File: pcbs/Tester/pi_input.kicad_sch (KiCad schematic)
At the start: 9 parts, among them J201 Raspberry_Pi_2_3, J202 Conn_01x04, J203 Conn_01x10, U201 SN74LVC4245APWR, U202 SN74LVC4245APWR, U203 SN74LVC4245APWR

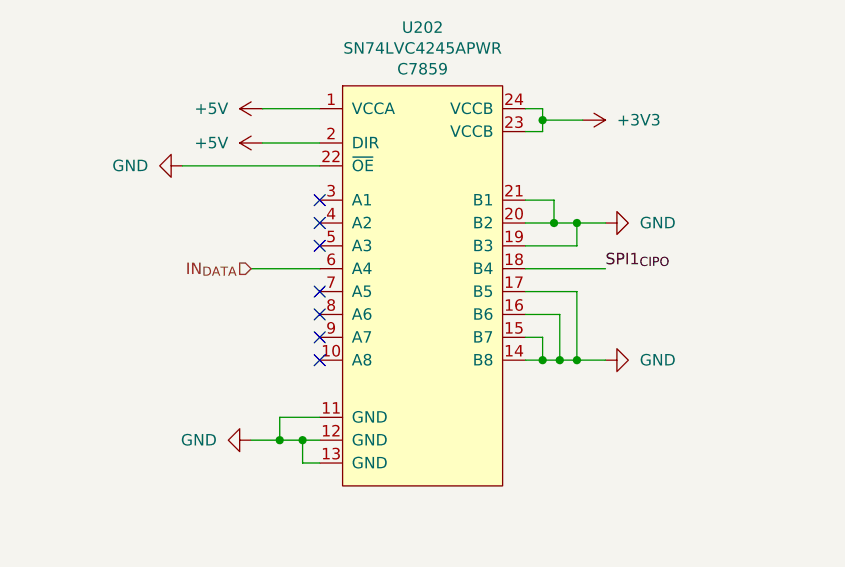
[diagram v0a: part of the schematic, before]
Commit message: Fix Tester board (#49)
The 'input' level shifter on the Tester board had the wrong set of pins connected to ground (copy paste error from the 'output' level shifters). This meant that the IC could effectively short circuit and become very hot. Switch over the ground and floating pins, to reflect how the inputs and outputs are for this IC.

Closes #47
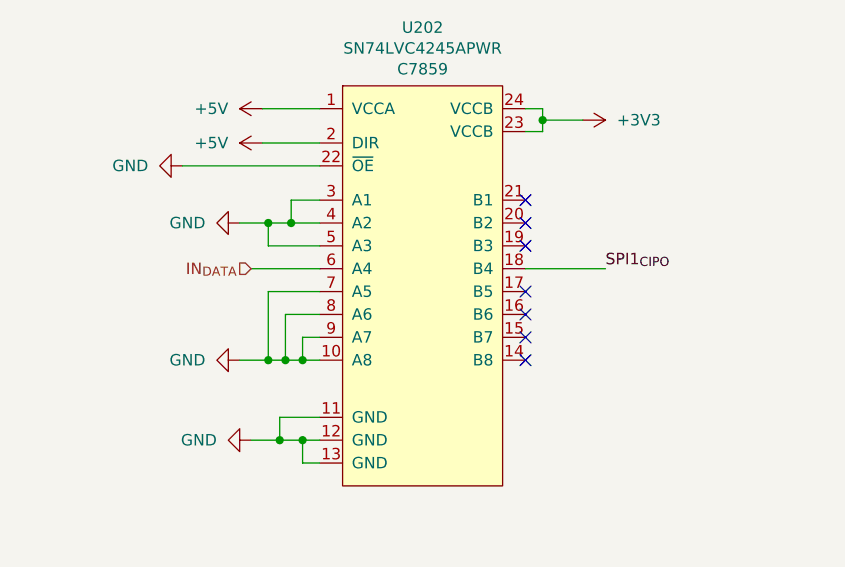
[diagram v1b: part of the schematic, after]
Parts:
- J203: footprint (none) -> Connector_PinHeader_2.54mm:PinHeader_1x10_P2.54mm_Vertical
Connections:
- net GND: now also U202.10 (A8), U202.3 (A1), U202.4 (A2), U202.5 (A3), U202.7 (A5), U202.8 (A6), U202.9 (A7); no longer U202.14 (B8), U202.15 (B7), U202.16 (B6), U202.17 (B5), U202.19 (B3), U202.20 (B2), U202.21 (B1)
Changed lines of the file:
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@@
   (junction (at 150.495 137.795) (diameter 0) (color 0 0 0 0)
   )
-  (junction (at 183.515 128.905) (diameter 0) (color 0 0 0 0)
+  (junction (at 149.225 128.905) (diameter 0) (color 0 0 0 0)
   )
   (junction (at 71.12 130.81) (diameter 0) (color 0 0 0 0)
@@
   (junction (at 74.93 130.81) (diameter 0) (color 0 0 0 0)
   )
-  (junction (at 183.515 113.665) (diameter 0) (color 0 0 0 0)
+  (junction (at 149.225 113.665) (diameter 0) (color 0 0 0 0)
   )
   (junction (at 76.2 130.81) (diameter 0) (color 0 0 0 0)
   )
-  (junction (at 180.975 113.665) (diameter 0) (color 0 0 0 0)
-  )
-  (junction (at 181.61 128.905) (diameter 0) (color 0 0 0 0)
-  )
-  (junction (at 179.705 128.905) (diameter 0) (color 0 0 0 0)
+  (junction (at 151.765 113.665) (diameter 0) (color 0 0 0 0)
+  )
+  (junction (at 151.13 128.905) (diameter 0) (color 0 0 0 0)
+  )
+  (junction (at 153.035 128.905) (diameter 0) (color 0 0 0 0)
   )
   (junction (at 229.87 128.27) (diameter 0) (color 0 0 0 0)
@@
   (junction (at 179.705 102.235) (diameter 0) (color 0 0 0 0)
   )
-  (no_connect (at 154.94 128.905))
   (no_connect (at 96.52 100.33))
-  (no_connect (at 154.94 113.665))
-  (no_connect (at 154.94 121.285))
-  (no_connect (at 154.94 123.825))
+  (no_connect (at 177.8 116.205))
+  (no_connect (at 177.8 121.285))
+  (no_connect (at 177.8 123.825))
+  (no_connect (at 177.8 113.665))
   (no_connect (at 55.88 100.33))
   (no_connect (at 234.315 50.8))
-  (no_connect (at 154.94 126.365))
   (no_connect (at 55.88 77.47))
   (no_connect (at 234.315 53.34))
-  (no_connect (at 154.94 111.125))
   (no_connect (at 55.88 80.01))
   (no_connect (at 234.315 48.26))
@@
   (no_connect (at 234.315 55.88))
   (no_connect (at 234.315 66.04))
-  (no_connect (at 154.94 116.205))
+  (no_connect (at 177.8 111.125))
   (no_connect (at 96.52 95.25))
+  (no_connect (at 177.8 128.905))
+  (no_connect (at 177.8 126.365))
   (bus_entry (at 144.145 53.975) (size 2.54 -2.54)
     (stroke (width 0) (type default) (color 0 0 0 0))
@@
     (stroke (width 0) (type default) (color 0 0 0 0))
   )
-  (wire (pts (xy 180.975 111.125) (xy 180.975 113.665))
+  (wire (pts (xy 151.765 111.125) (xy 151.765 113.665))
     (stroke (width 0) (type default) (color 0 0 0 0))
   )
@@
     (stroke (width 0) (type default) (color 0 0 0 0))
   )
-  (wire (pts (xy 177.8 113.665) (xy 180.975 113.665))
+  (wire (pts (xy 154.94 113.665) (xy 151.765 113.665))
     (stroke (width 0) (type default) (color 0 0 0 0))
   )
@@
     (stroke (width 0) (type default) (color 0 0 0 0))
   )
-  (wire (pts (xy 177.8 121.285) (xy 183.515 121.285))
+  (wire (pts (xy 154.94 121.285) (xy 149.225 121.285))
     (stroke (width 0) (type default) (color 0 0 0 0))
   )
@@
     (stroke (width 0) (type default) (color 0 0 0 0))
   )
-  (wire (pts (xy 180.975 113.665) (xy 183.515 113.665))
-    (stroke (width 0) (type default) (color 0 0 0 0))
-  )
-  (wire (pts (xy 181.61 123.825) (xy 181.61 128.905))
+  (wire (pts (xy 151.765 113.665) (xy 149.225 113.665))
+    (stroke (width 0) (type default) (color 0 0 0 0))
+  )
+  (wire (pts (xy 151.13 123.825) (xy 151.13 128.905))
     (stroke (width 0) (type default) (color 0 0 0 0))
   )
@@
     (stroke (width 0) (type default) (color 0 0 0 0))
   )
-  (wire (pts (xy 181.61 128.905) (xy 183.515 128.905))
+  (wire (pts (xy 151.13 128.905) (xy 149.225 128.905))
     (stroke (width 0) (type default) (color 0 0 0 0))
   )
@@
     (stroke (width 0) (type default) (color 0 0 0 0))
   )
-  (wire (pts (xy 183.515 128.905) (xy 186.69 128.905))
+  (wire (pts (xy 149.225 128.905) (xy 146.05 128.905))
     (stroke (width 0) (type default) (color 0 0 0 0))
   )
@@
     (stroke (width 0) (type default) (color 0 0 0 0))
   )
-  (wire (pts (xy 183.515 116.205) (xy 183.515 113.665))
+  (wire (pts (xy 149.225 116.205) (xy 149.225 113.665))
     (stroke (width 0) (type default) (color 0 0 0 0))
   )
@@
     (stroke (width 0) (type default) (color 0 0 0 0))
   )
-  (wire (pts (xy 179.705 126.365) (xy 179.705 128.905))
+  (wire (pts (xy 153.035 126.365) (xy 153.035 128.905))
     (stroke (width 0) (type default) (color 0 0 0 0))
   )
@@
     (stroke (width 0) (type default) (color 0 0 0 0))
   )
-  (wire (pts (xy 183.515 121.285) (xy 183.515 128.905))
+  (wire (pts (xy 149.225 121.285) (xy 149.225 128.905))
     (stroke (width 0) (type default) (color 0 0 0 0))
   )
@@
     (stroke (width 0) (type default) (color 0 0 0 0))
   )
-  (wire (pts (xy 177.8 123.825) (xy 181.61 123.825))
+  (wire (pts (xy 154.94 123.825) (xy 151.13 123.825))
     (stroke (width 0) (type default) (color 0 0 0 0))
   )
@@
     (stroke (width 0) (type default) (color 0 0 0 0))
   )
-  (wire (pts (xy 179.705 128.905) (xy 181.61 128.905))
-    (stroke (width 0) (type default) (color 0 0 0 0))
-  )
-  (wire (pts (xy 183.515 113.665) (xy 186.69 113.665))
+  (wire (pts (xy 153.035 128.905) (xy 151.13 128.905))
+    (stroke (width 0) (type default) (color 0 0 0 0))
+  )
+  (wire (pts (xy 149.225 113.665) (xy 146.05 113.665))
     (stroke (width 0) (type default) (color 0 0 0 0))
   )
@@
     (stroke (width 0) (type default) (color 0 0 0 0))
   )
-  (wire (pts (xy 177.8 116.205) (xy 183.515 116.205))
+  (wire (pts (xy 154.94 116.205) (xy 149.225 116.205))
     (stroke (width 0) (type default) (color 0 0 0 0))
   )
@@
     (stroke (width 0) (type default) (color 0 0 0 0))
   )
-  (wire (pts (xy 177.8 111.125) (xy 180.975 111.125))
+  (wire (pts (xy 154.94 111.125) (xy 151.765 111.125))
     (stroke (width 0) (type default) (color 0 0 0 0))
   )
@@
     (stroke (width 0) (type default) (color 0 0 0 0))
   )
-  (wire (pts (xy 177.8 128.905) (xy 179.705 128.905))
+  (wire (pts (xy 154.94 128.905) (xy 153.035 128.905))
     (stroke (width 0) (type default) (color 0 0 0 0))
   )
@@
     (stroke (width 0) (type default) (color 0 0 0 0))
   )
-  (wire (pts (xy 177.8 126.365) (xy 179.705 126.365))
+  (wire (pts (xy 154.94 126.365) (xy 153.035 126.365))
     (stroke (width 0) (type default) (color 0 0 0 0))
   )
@@
     (pin "1")
   )
-  (symbol (lib_id "power:GND") (at 186.69 113.665 90) (unit 1)
-    (in_bom yes) (on_board yes) (fields_autoplaced)
-    (property "Reference" "#PWR0223" (id 0) (at 193.04 113.665 0)
-      (effects (font (size 1.27 1.27)) hide)
-    )
-    (property "Value" "GND" (id 1) (at 190.5 113.6649 90)
+  (symbol (lib_id "power:GND") (at 146.05 113.665 270) (mirror x) (unit 1)
+    (in_bom yes) (on_board yes) (fields_autoplaced)
+    (property "Reference" "#PWR0223" (id 0) (at 139.7 113.665 0)
+      (effects (font (size 1.27 1.27)) hide)
+    )
+    (property "Value" "GND" (id 1) (at 142.24 113.6649 90)
       (effects (font (size 1.27 1.27)) (justify right))
     )
-    (property "Footprint" "" (id 2) (at 186.69 113.665 0)
-      (effects (font (size 1.27 1.27)) hide)
-    )
-    (property "Datasheet" "" (id 3) (at 186.69 113.665 0)
+    (property "Footprint" "" (id 2) (at 146.05 113.665 0)
+      (effects (font (size 1.27 1.27)) hide)
+    )
+    (property "Datasheet" "" (id 3) (at 146.05 113.665 0)
       (effects (font (size 1.27 1.27)) hide)
     )
@@
     (pin "4")
   )
-  (symbol (lib_id "power:GND") (at 186.69 128.905 90) (unit 1)
-    (in_bom yes) (on_board yes) (fields_autoplaced)
-    (property "Reference" "#PWR0224" (id 0) (at 193.04 128.905 0)
-      (effects (font (size 1.27 1.27)) hide)
-    )
-    (property "Value" "GND" (id 1) (at 190.5 128.9049 90)
+  (symbol (lib_id "power:GND") (at 146.05 128.905 270) (mirror x) (unit 1)
+    (in_bom yes) (on_board yes) (fields_autoplaced)
+    (property "Reference" "#PWR0224" (id 0) (at 139.7 128.905 0)
+      (effects (font (size 1.27 1.27)) hide)
+    )
+    (property "Value" "GND" (id 1) (at 142.24 128.9049 90)
       (effects (font (size 1.27 1.27)) (justify right))
     )
-    (property "Footprint" "" (id 2) (at 186.69 128.905 0)
-      (effects (font (size 1.27 1.27)) hide)
-    )
-    (property "Datasheet" "" (id 3) (at 186.69 128.905 0)
+    (property "Footprint" "" (id 2) (at 146.05 128.905 0)
+      (effects (font (size 1.27 1.27)) hide)
+    )
+    (property "Datasheet" "" (id 3) (at 146.05 128.905 0)
       (effects (font (size 1.27 1.27)) hide)
     )
@@
       (effects (font (size 1.27 1.27)) (justify left))
     )
-    (property "Footprint" "" (id 2) (at 140.335 166.37 0)
-      (effects (font (size 1.27 1.27)) hide)
-    )
+    (property "Footprint" "Connector_PinHeader_2.54mm:PinHeader_1x10_P2.54mm_Vertical" (id 2) (at 140.335 166.37 0)
+      (effects (font (size 1.27 1.27)) hide)
+    )
